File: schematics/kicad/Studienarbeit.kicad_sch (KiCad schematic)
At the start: 78 parts, among them J1 AudioJack3, J2 Conn_01x18, J3 Conn_01x18, J4 Conn_01x01_Pin, J5 Conn_01x01_Pin, J6 Conn_01x01_Pin, J7 Conn_01x01_Pin, U2 PCM5102, U3 MCP6001-OT, U4 MCP6001-OT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

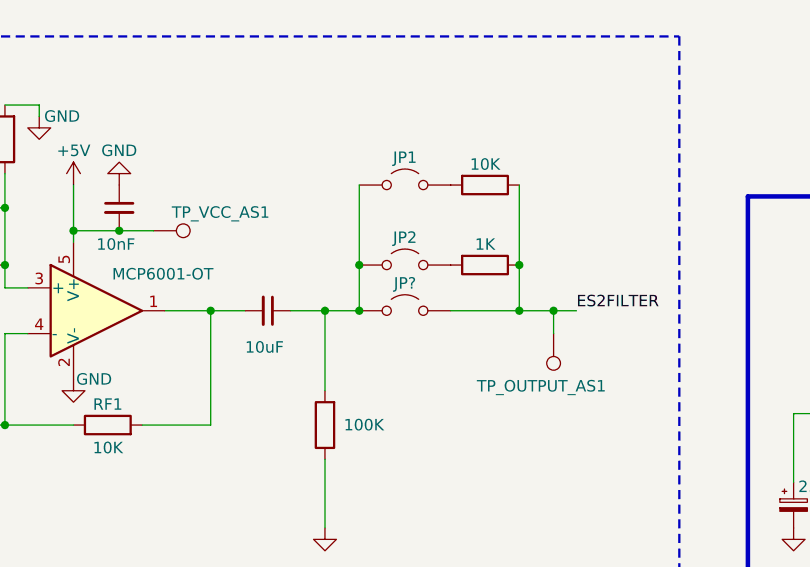
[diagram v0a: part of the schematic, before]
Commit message: KiCad: rerouted the jumpers.
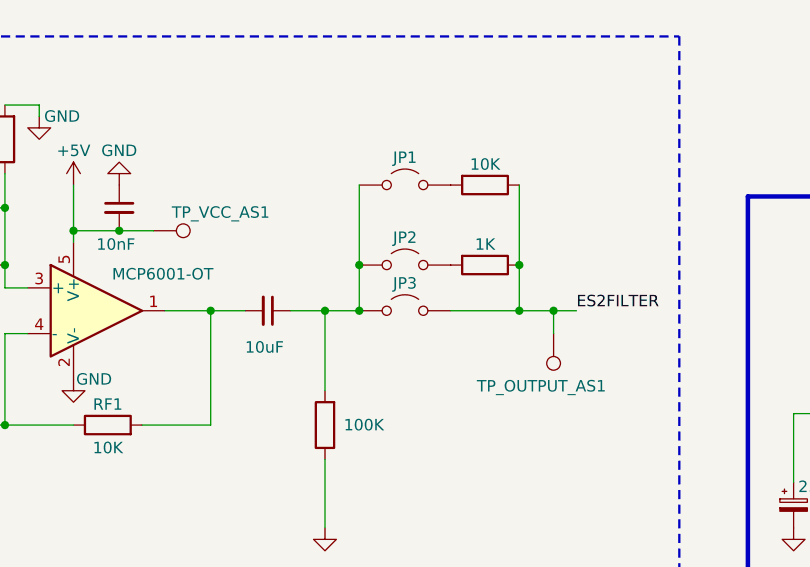
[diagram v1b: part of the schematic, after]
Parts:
- removed JP?: Jumper_2_Open, symbol Jumper:Jumper_2_Open
- added JP3: Jumper_2_Open, Jumper:SolderJumper-2_P1.3mm_Open_Pad1.0x1.5mm, symbol Jumper:Jumper_2_Open
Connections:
- net ES2FILTER: now also JP3.2 (B)
- net at C_COUPLING_AMPSTAGE1.1, JP1.1 (A), JP2.1 (A)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: now also JP3.1 (A)
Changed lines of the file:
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@@
 	)
 	(junction
+		(at 269.24 109.22)
+		(diameter 0)
+		(color 0 0 0 0)
+	)
+	(junction
 		(at 81.28 187.96)
 		(diameter 0)
@@
 	)
 	(junction
-		(at 269.24 109.22)
-		(diameter 0)
-		(color 0 0 0 0)
-	)
-	(junction
 		(at 375.92 175.26)
 		(diameter 0)
@@
 	)
 	(symbol
+		(lib_id "Jumper:Jumper_2_Open")
+		(at 274.32 109.22 0)
+		(unit 1)
+		(exclude_from_sim yes)
+		(in_bom yes)
+		(on_board yes)
+		(dnp no)
+		(property "Reference" "JP3"
+			(at 274.32 106.172 0)
+			(effects
+				(font
+					(size 1.27 1.27)
+				)
+			)
+		)
+		(property "Value" "Jumper_2_Open"
+			(at 274.32 105.41 0)
+			(effects
+				(font
+					(size 1.27 1.27)
+				)
+				(hide yes)
+			)
+		)
+		(property "Footprint" "Jumper:SolderJumper-2_P1.3mm_Open_Pad1.0x1.5mm"
+			(at 274.32 109.22 0)
+			(effects
+				(font
+					(size 1.27 1.27)
+				)
+				(hide yes)
+			)
+		)
+		(property "Datasheet" "~"
+			(at 274.32 109.22 0)
+			(effects
+				(font
+					(size 1.27 1.27)
+				)
+				(hide yes)
+			)
+		)
+		(property "Description" "Jumper, 2-pole, open"
+			(at 274.32 109.22 0)
+			(effects
+				(font
+					(size 1.27 1.27)
+				)
+				(hide yes)
+			)
+		)
+		(pin "1"
+		)
+		(pin "2"
+		)
+		(instances
+			(project "Studienarbeit"
+				(path "/e1f471d3-f850-4433-b54a-c7e6f7857097"
+					(reference "JP3")
+					(unit 1)
+				)
+			)
+		)
+	)
+	(symbol
 		(lib_id "Device:R")
 		(at 220.98 121.92 90)
@@
 					(unit 1)
 				)
-			)
-		)
-	)
-	(symbol
-		(lib_id "Jumper:Jumper_2_Open")
-		(at 274.32 109.22 0)
-		(unit 1)
-		(exclude_from_sim yes)
-		(in_bom yes)
-		(on_board yes)
-		(dnp no)
-		(property "Reference" "JP?"
-			(at 274.32 106.172 0)
-			(effects
-				(font
-					(size 1.27 1.27)
-				)
-			)
-		)
-		(property "Value" "Jumper_2_Open"
-			(at 274.32 105.41 0)
-			(effects
-				(font
-					(size 1.27 1.27)
-				)
-				(hide yes)
-			)
-		)
-		(property "Footprint" ""
-			(at 274.32 109.22 0)
-			(effects
-				(font
-					(size 1.27 1.27)
-				)
-				(hide yes)
-			)
-		)
-		(property "Datasheet" "~"
-			(at 274.32 109.22 0)
-			(effects
-				(font
-					(size 1.27 1.27)
-				)
-				(hide yes)
-			)
-		)
-		(property "Description" "Jumper, 2-pole, open"
-			(at 274.32 109.22 0)
-			(effects
-				(font
-					(size 1.27 1.27)
-				)
-				(hide yes)
-			)
-		)
-		(pin "1"
-		)
-		(pin "2"
-		)
-		(instances
-			(project ""
-				(path "/e1f471d3-f850-4433-b54a-c7e6f7857097"
-					(reference "JP?")
-					(unit 1)
-				)

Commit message: Updated PCB based on feedback (1).
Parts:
- added C_IN_+15V_1: 10uF, Capacitor_SMD:C_1206_3216Metric_Pad1.33x1.80mm_HandSolder, symbol Device:C_Small
- added D1: D_Schottky, Diode_SMD:D_SMC-RM10_Universal_Handsoldering, symbol Device:D_Schottky
- added D2: 1N4148, Diode_THT:D_DO-35_SOD27_P7.62mm_Horizontal, symbol Diode:1N4148
- added DEBUG1: 0, Resistor_SMD:R_0805_2012Metric_Pad1.20x1.40mm_HandSolder, symbol Device:R
- added STATUS_LED1: 330, Resistor_SMD:R_0805_2012Metric_Pad1.20x1.40mm_HandSolder, symbol Device:R
- LS1: footprint TerminalBlock:TerminalBlock_Xinya_XY308-2.54-2P_1x02_P2.54mm_Horizontal -> TerminalBlock:TerminalBlock_bornier-2_P5.08mm
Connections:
- net SYSTEMCTL is gone; now on net GND: U6.1 (SHUTDOWN)
- net XSMT/MUTE is gone; now on net GND: U2.17 (XSMT)
- net +15V: now also D1.2 (A); no longer C_INPUT_LDO1.2, U7.1 (IN)
- net +5V: now also D2.2 (A)
- net GND: now also C_IN_+15V_1.2, STATUS_LED1.1
- net at TP_OUTPUT_AS2.1, U5.3: now also DEBUG1.2; no longer RF2.2, U3.1
- net ES2FILTER renamed Filter_IN
- net Filter_IN: no longer C_IN_AMPSTAGE1.1, J6.1 (Pin_1)
- net SCK: no longer names the net of U2.12 (SCK)
- new net: DEBUG1.1, RF2.2, U3.1
- new net: C_INPUT_LDO1.2, C_IN_+15V_1.1, D1.1 (K), U7.1 (IN)
- new net: D2.1 (K), STATUS_LED1.2
- new net Filter_OUT: C_IN_AMPSTAGE1.1, J6.1 (Pin_1)
- no-connect marks 1 -> 33
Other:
- moved on the sheet: TP_LM2940_+5V1, TP_OUTPUT_AS2

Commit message: Updated the PCB with prof feedback.
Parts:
- added C_INPUT_TPA1: 10uF, Capacitor_SMD:C_1206_3216Metric_Pad1.33x1.80mm_HandSolder, symbol Device:C_Small
- added C_INPUT_TPA2: 100nF, Capacitor_SMD:C_1206_3216Metric_Pad1.33x1.80mm_HandSolder, symbol Device:C_Small
- added JP4, JP5: Jumper_2_Open, Jumper:SolderJumper-2_P1.3mm_Open_Pad1.0x1.5mm, symbol Jumper:Jumper_2_Open
- D1: footprint Diode_SMD:D_SMC-RM10_Universal_Handsoldering -> Diode_SMD:Nexperia_CFP3_SOD-123W
- D2: footprint Diode_THT:D_DO-35_SOD27_P7.62mm_Horizontal -> Diode_SMD:D_0805_2012Metric
- J4, J5, J6, J7: footprint TestPoint:TestPoint_THTPad_2.0x2.0mm_Drill1.0mm -> TestPoint:FestoBoard_Drill_Hole
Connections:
- net +5V: now also C_INPUT_TPA1.1, C_INPUT_TPA2.1
- net GND: now also U7.4 (GND), C_INPUT_TPA1.2, C_INPUT_TPA2.2, JP4.1 (A), JP5.1 (A); no longer U2.17 (XSMT), U6.1 (SHUTDOWN)
- new net: JP5.2 (B), U6.1 (SHUTDOWN)
- new net: JP4.2 (B), U2.17 (XSMT)
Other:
- moved on the sheet: TP_VDD_TPA1, TP_Vo+_TPA1, TP_Vo-_TPA1

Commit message: Updated the parts list.
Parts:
- C1_APS_PCM5102, C_COUPLING_AMPSTAGE1, C_GND_AMPSTAGE1, C_GND_AMPSTAGE2, C_GND_AMPSTAGE3, C_INPUT_TPA1, C_IN_+15V_1, C_IN_AMPSTAGE1: OC_Mouser (none) -> 581-KAF31GR71C106KU
- C1_CPPS_PCM1, C1_DPS_PCM1, C2_APS_PCM5102, C2_DPS_PCM1, C_INPUT_TPA2, C_SE/BTL_TPA1: Comments (none) -> 0.1uF = 100nF; OC_Mouser (none) -> 581-KAF31BR71H104KT
- C2_CPPS_PCM1, CA_PCM5102, CB_TPA1: OC_Mouser (none) -> 581-KAF31GR71E225KU
- CC_TPA711: Comments (none) -> Unsure, maybe find alternative, must also be polarized???; OC_Mouser (none) -> 81-GRM32ER60G337ME5K
- CF_TPA711: OC_Mouser (none) -> 581-12061A5R0CAT2A
- CG1_PCM5102, CG2_PCM5102: OC_Mouser (none) -> 81-GRM31BR72E223KW01
- CI_TPA711, C_INPUT_LDO1: OC_Mouser (none) -> 581-KAF31ER71H474KU
- C_COUPLING_AMPSTAGE2, C_COUPLING_AMPSTAGE3, C_COUPLING_AMPSTAGE4: OC_Mouser (none) -> 581-KGM31GCG2J103JU
- C_OUTPUT_LDO1: OC_Mouser (none) -> 81-GCM31CR70J226ME3L
- D1: footprint Diode_SMD:Nexperia_CFP3_SOD-123W -> Diode_SMD:D_SOD-123F; OC_Mouser (none) -> 621-1N5819HW-F
- D2: footprint Diode_SMD:D_0805_2012Metric -> Diode_SMD:D_SOD-123F; Comments (none) -> Doesn't look like an LED to me. What replacement to put?; OC_Mouser (none) -> 78-1N4148W-HG3_A-08
- J1: Comments (none) -> Mouser component is thruhole while footrpint is with pads. 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; OC_Mouser (none) -> 179-SJ3-35083A-TR
- J2, J3: Comments (none) -> No idea
- J4, J5, J6, J7: Comments (none) -> Screws? Washers? Do we have to order?
- JP1, JP2, JP3, JP4, JP5, TP_AVDD_PCM1, TP_BCK1, TP_CPVDD_PCM1, TP_DIN1, TP_DVDD_PCM1, TP_GND_ESP32, TP_INPUTBIAS_AS1, TP_INPUTBIAS_AS2, TP_LM2940_+5V1, TP_LRCK1, TP_OUTPUT_AS1, TP_OUTPUT_AS2, TP_OUTPUT_BUFFER1, TP_VCC_AS1, TP_VCC_AS2, TP_VCC_Buffer1, TP_VDD_TPA1, TP_Vo+_TPA1, TP_Vo-_TPA1: OC_Mouser (none) -> X
- LS1: OC_Mouser (none) -> 651-1729128
- R1, R3, R4, R_COUPLING_AMPSTAGE2: footprint LED_SMD:LED_0805_2012Metric_Pad1.15x1.40mm_HandSolder -> Resistor_SMD:R_0805_2012Metric_Pad1.20x1.40mm_HandSolder; OC_Mouser (none) -> 708-RNHT0805BTE10K0
- R11: OC_Mouser (none) -> 652-CR0805AFX1001EAS
- R12, R13: OC_Mouser (none) -> 603-RT0805BRE07100KL
- R2, RI_TPA711: OC_Mouser (none) -> 708-RNHT0805BTE10K0
- RF1, RF2: value 10K -> 5K; OC_Mouser (none) -> 71-RCA08055K10FKEA
- RF_TPA711: OC_Mouser (none) -> 71-CRCW08051503DT
- RG1: value 200k -> 100k; footprint LED_SMD:LED_0805_2012Metric_Pad1.15x1.40mm_HandSolder -> Resistor_SMD:R_0805_2012Metric_Pad1.20x1.40mm_HandSolder; OC_Mouser (none) -> 603-RT0805BRE07100KL
- RG2: value 200K -> 100K; OC_Mouser (none) -> 603-RT0805BRE07100KL
- ROUTDACL1, ROUTDACR1: OC_Mouser (none) -> 71-RCS0805470KJNEA
- R_COUPLING_AMPSTAGE1: footprint LED_SMD:LED_0805_2012Metric_Pad1.15x1.40mm_HandSolder -> Resistor_SMD:R_0805_2012Metric_Pad1.20x1.40mm_HandSolder; OC_Mouser (none) -> 603-RT0805BRE07100KL
- R_COUPLING_AMPSTAGE3: footprint LED_SMD:LED_0805_2012Metric_Pad1.15x1.40mm_HandSolder -> Resistor_SMD:R_0805_2012Metric_Pad1.20x1.40mm_HandSolder; OC_Mouser (none) -> 652-CR0805AFX1001EAS
- STATUS_LED1: OC_Mouser (none) -> 594-MCU08050C3300FP5
- U2: OC_Mouser (none) -> 595-PCM5102AQPWRQ1
- U3, U4, U5: OC_Mouser (none) -> 579-MCP6001UT-I/OT
- U6: OC_Mouser (none) -> 595-TPA711DR
- U7: OC_Mouser (none) -> 926-LM2940CT50LF01
